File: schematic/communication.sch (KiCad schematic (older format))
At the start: 12 parts

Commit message: prototype footprint and placement test
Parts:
- C10, C9: renamed from C?; footprint (none) -> Capacitor_SMD:C_0805_2012Metric_Pad1.15x1.40mm_HandSolder
- J18: renamed from J?; footprint (none) -> Connector_PinHeader_2.54mm:PinHeader_1x02_P2.54mm_Vertical
- J19: renamed from J?; footprint (none) -> Connector_JST:JST_XH_B2B-XH-AM_1x02_P2.50mm_Vertical
- R17, R18, R19, R20, R21, R22, R23: renamed from R?; footprint (none) -> Resistor_SMD:R_0805_2012Metric_Pad1.15x1.40mm_HandSolder
- U5: renamed from U?; footprint (none) -> Package_SO:SOIC-8_3.9x4.9mm_P1.27mm
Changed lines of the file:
@@
 P 5400 3900
 AR Path="/5EFB8F98" Ref="U?"  Part="1"
-AR Path="/5EFB4D6F/5EFB8F98" Ref="U?"  Part="1"
-F 0 "U?" H 5500 4500 50  0000 C CNN
+AR Path="/5EFB4D6F/5EFB8F98" Ref="U5"  Part="1"
+F 0 "U5" H 5500 4500 50  0000 C CNN
 F 1 "MAX485E" H 5600 4400 50  0000 C CNN
-F 2 "" H 5400 3200 50  0001 C CNN
+F 2 "Package_SO:SOIC-8_3.9x4.9mm_P1.27mm" H 5400 3200 50  0001 C CNN
 F 3 "https://datasheets.maximintegrated.com/en/ds/MAX1487E-MAX491E.pdf" H 5400 3950 50  0001 C CNN
 	1    5400 3900
@@
 P 7150 3800
 AR Path="/5EFB8F9E" Ref="J?"  Part="1"
-AR Path="/5EFB4D6F/5EFB8F9E" Ref="J?"  Part="1"
-F 0 "J?" H 7230 3792 50  0000 L CNN
+AR Path="/5EFB4D6F/5EFB8F9E" Ref="J19"  Part="1"
+F 0 "J19" H 7230 3792 50  0000 L CNN
 F 1 "Conn_01x02" H 7230 3701 50  0000 L CNN
-F 2 "" H 7150 3800 50  0001 C CNN
+F 2 "Connector_JST:JST_XH_B2B-XH-AM_1x02_P2.50mm_Vertical" H 7150 3800 50  0001 C CNN
 F 3 "~" H 7150 3800 50  0001 C CNN
 	1    7150 3800
@@
 P 6200 4400
 AR Path="/5EFB8FA4" Ref="#PWR?"  Part="1"
-AR Path="/5EFB4D6F/5EFB8FA4" Ref="#PWR?"  Part="1"
-F 0 "#PWR?" H 6200 4250 50  0001 C CNN
+AR Path="/5EFB4D6F/5EFB8FA4" Ref="#PWR060"  Part="1"
+F 0 "#PWR060" H 6200 4250 50  0001 C CNN
 F 1 "+3.3V" H 6215 4573 50  0000 C CNN
 F 2 "" H 6200 4400 50  0001 C CNN
@@
 P 6200 3500
 AR Path="/5EFB8FAA" Ref="#PWR?"  Part="1"
-AR Path="/5EFB4D6F/5EFB8FAA" Ref="#PWR?"  Part="1"
-F 0 "#PWR?" H 6200 3250 50  0001 C CNN
+AR Path="/5EFB4D6F/5EFB8FAA" Ref="#PWR059"  Part="1"
+F 0 "#PWR059" H 6200 3250 50  0001 C CNN
 F 1 "GND" H 6205 3327 50  0000 C CNN
 F 2 "" H 6200 3500 50  0001 C CNN
@@
 P 6200 3650
 AR Path="/5EFB8FB0" Ref="R?"  Part="1"
-AR Path="/5EFB4D6F/5EFB8FB0" Ref="R?"  Part="1"
-F 0 "R?" H 6270 3696 50  0000 L CNN
+AR Path="/5EFB4D6F/5EFB8FB0" Ref="R21"  Part="1"
+F 0 "R21" H 6270 3696 50  0000 L CNN
 F 1 "20K" H 6270 3605 50  0000 L CNN
-F 2 "" V 6130 3650 50  0001 C CNN
+F 2 "Resistor_SMD:R_0805_2012Metric_Pad1.15x1.40mm_HandSolder" V 6130 3650 50  0001 C CNN
 F 3 "~" H 6200 3650 50  0001 C CNN
 	1    6200 3650
@@
 P 6200 4250
 AR Path="/5EFB8FB6" Ref="R?"  Part="1"
-AR Path="/5EFB4D6F/5EFB8FB6" Ref="R?"  Part="1"
-F 0 "R?" H 6270 4296 50  0000 L CNN
+AR Path="/5EFB4D6F/5EFB8FB6" Ref="R22"  Part="1"
+F 0 "R22" H 6270 4296 50  0000 L CNN
 F 1 "20K" H 6270 4205 50  0000 L CNN
-F 2 "" V 6130 4250 50  0001 C CNN
+F 2 "Resistor_SMD:R_0805_2012Metric_Pad1.15x1.40mm_HandSolder" V 6130 4250 50  0001 C CNN
 F 3 "~" H 6200 4250 50  0001 C CNN
 	1    6200 4250
@@
 P 5400 4500
 AR Path="/5EFB8FBD" Ref="#PWR?"  Part="1"
-AR Path="/5EFB4D6F/5EFB8FBD" Ref="#PWR?"  Part="1"
-F 0 "#PWR?" H 5400 4250 50  0001 C CNN
+AR Path="/5EFB4D6F/5EFB8FBD" Ref="#PWR058"  Part="1"
+F 0 "#PWR058" H 5400 4250 50  0001 C CNN
 F 1 "GND" H 5405 4327 50  0000 C CNN
 F 2 "" H 5400 4500 50  0001 C CNN
@@
 P 6450 3450
 AR Path="/5EFB8FC6" Ref="R?"  Part="1"
-AR Path="/5EFB4D6F/5EFB8FC6" Ref="R?"  Part="1"
-F 0 "R?" H 6520 3496 50  0000 L CNN
+AR Path="/5EFB4D6F/5EFB8FC6" Ref="R23"  Part="1"
+F 0 "R23" H 6520 3496 50  0000 L CNN
 F 1 "120" H 6520 3405 50  0000 L CNN
-F 2 "" V 6380 3450 50  0001 C CNN
+F 2 "Resistor_SMD:R_0805_2012Metric_Pad1.15x1.40mm_HandSolder" V 6380 3450 50  0001 C CNN
 F 3 "~" H 6450 3450 50  0001 C CNN
 	1    6450 3450
@@
 P 4750 3550
 AR Path="/5EFB8FCF" Ref="R?"  Part="1"
-AR Path="/5EFB4D6F/5EFB8FCF" Ref="R?"  Part="1"
-F 0 "R?" H 4820 3596 50  0000 L CNN
+AR Path="/5EFB4D6F/5EFB8FCF" Ref="R20"  Part="1"
+F 0 "R20" H 4820 3596 50  0000 L CNN
 F 1 "10K" H 4820 3505 50  0000 L CNN
-F 2 "" V 4680 3550 50  0001 C CNN
+F 2 "Resistor_SMD:R_0805_2012Metric_Pad1.15x1.40mm_HandSolder" V 4680 3550 50  0001 C CNN
 F 3 "~" H 4750 3550 50  0001 C CNN
 	1    4750 3550
@@
 P 4600 3550
 AR Path="/5EFB8FD5" Ref="R?"  Part="1"
-AR Path="/5EFB4D6F/5EFB8FD5" Ref="R?"  Part="1"
-F 0 "R?" H 4670 3596 50  0000 L CNN
+AR Path="/5EFB4D6F/5EFB8FD5" Ref="R19"  Part="1"
+F 0 "R19" H 4670 3596 50  0000 L CNN
 F 1 "10K" H 4670 3505 50  0000 L CNN
-F 2 "" V 4530 3550 50  0001 C CNN
+F 2 "Resistor_SMD:R_0805_2012Metric_Pad1.15x1.40mm_HandSolder" V 4530 3550 50  0001 C CNN
 F 3 "~" H 4600 3550 50  0001 C CNN
 	1    4600 3550
@@
 P 4450 3550
 AR Path="/5EFB8FDB" Ref="R?"  Part="1"
-AR Path="/5EFB4D6F/5EFB8FDB" Ref="R?"  Part="1"
-F 0 "R?" H 4520 3596 50  0000 L CNN
+AR Path="/5EFB4D6F/5EFB8FDB" Ref="R18"  Part="1"
+F 0 "R18" H 4520 3596 50  0000 L CNN
 F 1 "10K" H 4520 3505 50  0000 L CNN
-F 2 "" V 4380 3550 50  0001 C CNN
+F 2 "Resistor_SMD:R_0805_2012Metric_Pad1.15x1.40mm_HandSolder" V 4380 3550 50  0001 C CNN
 F 3 "~" H 4450 3550 50  0001 C CNN
 	1    4450 3550
@@
 P 4300 3550
 AR Path="/5EFB8FE1" Ref="R?"  Part="1"
-AR Path="/5EFB4D6F/5EFB8FE1" Ref="R?"  Part="1"
-F 0 "R?" H 4370 3596 50  0000 L CNN
+AR Path="/5EFB4D6F/5EFB8FE1" Ref="R17"  Part="1"
+F 0 "R17" H 4370 3596 50  0000 L CNN
 F 1 "10K" H 4370 3505 50  0000 L CNN
-F 2 "" V 4230 3550 50  0001 C CNN
+F 2 "Resistor_SMD:R_0805_2012Metric_Pad1.15x1.40mm_HandSolder" V 4230 3550 50  0001 C CNN
 F 3 "~" H 4300 3550 50  0001 C CNN
 	1    4300 3550
@@
 P 4550 3400
 AR Path="/5EFB9000" Ref="#PWR?"  Part="1"
-AR Path="/5EFB4D6F/5EFB9000" Ref="#PWR?"  Part="1"
-F 0 "#PWR?" H 4550 3250 50  0001 C CNN
+AR Path="/5EFB4D6F/5EFB9000" Ref="#PWR054"  Part="1"
+F 0 "#PWR054" H 4550 3250 50  0001 C CNN
 F 1 "+3.3V" H 4565 3573 50  0000 C CNN
 F 2 "" H 4550 3400 50  0001 C CNN
@@
 P 6900 3400
 AR Path="/5EFB9026" Ref="J?"  Part="1"
-AR Path="/5EFB4D6F/5EFB9026" Ref="J?"  Part="1"
-F 0 "J?" H 6872 3282 50  0000 R CNN
+AR Path="/5EFB4D6F/5EFB9026" Ref="J18"  Part="1"
+F 0 "J18" H 6872 3282 50  0000 R CNN
 F 1 "Conn_01x02_Male" H 6872 3373 50  0000 R CNN
-F 2 "" H 6900 3400 50  0001 C CNN
+F 2 "Connector_PinHeader_2.54mm:PinHeader_1x02_P2.54mm_Vertical" H 6900 3400 50  0001 C CNN
 F 3 "~" H 6900 3400 50  0001 C CNN
 	1    6900 3400
@@
 P 5350 2850
 AR Path="/5EFB900E" Ref="C?"  Part="1"
-AR Path="/5EFB4D6F/5EFB900E" Ref="C?"  Part="1"
-F 0 "C?" H 5465 2896 50  0000 L CNN
+AR Path="/5EFB4D6F/5EFB900E" Ref="C10"  Part="1"
+F 0 "C10" H 5465 2896 50  0000 L CNN
 F 1 "0.1uF" H 5465 2805 50  0000 L CNN
-F 2 "" H 5388 2700 50  0001 C CNN
+F 2 "Capacitor_SMD:C_0805_2012Metric_Pad1.15x1.40mm_HandSolder" H 5388 2700 50  0001 C CNN
 F 3 "~" H 5350 2850 50  0001 C CNN
 	1    5350 2850
@@
 P 4900 2850
 AR Path="/5EFB9008" Ref="C?"  Part="1"
-AR Path="/5EFB4D6F/5EFB9008" Ref="C?"  Part="1"
-F 0 "C?" H 5015 2896 50  0000 L CNN
+AR Path="/5EFB4D6F/5EFB9008" Ref="C9"  Part="1"
+F 0 "C9" H 5015 2896 50  0000 L CNN
 F 1 "10uF" H 5015 2805 50  0000 L CNN
-F 2 "" H 4938 2700 50  0001 C CNN
+F 2 "Capacitor_SMD:C_0805_2012Metric_Pad1.15x1.40mm_HandSolder" H 4938 2700 50  0001 C CNN
 F 3 "~" H 4900 2850 50  0001 C CNN
 	1    4900 2850
@@
 P 5150 2700
 AR Path="/5EFB9014" Ref="#PWR?"  Part="1"
-AR Path="/5EFB4D6F/5EFB9014" Ref="#PWR?"  Part="1"
-F 0 "#PWR?" H 5150 2550 50  0001 C CNN
+AR Path="/5EFB4D6F/5EFB9014" Ref="#PWR055"  Part="1"
+F 0 "#PWR055" H 5150 2550 50  0001 C CNN
 F 1 "+3.3V" H 5165 2873 50  0000 C CNN
 F 2 "" H 5150 2700 50  0001 C CNN
@@
 P 5150 3000
 AR Path="/5EFB901A" Ref="#PWR?"  Part="1"
-AR Path="/5EFB4D6F/5EFB901A" Ref="#PWR?"  Part="1"
-F 0 "#PWR?" H 5150 2750 50  0001 C CNN
+AR Path="/5EFB4D6F/5EFB901A" Ref="#PWR056"  Part="1"
+F 0 "#PWR056" H 5150 2750 50  0001 C CNN
 F 1 "GND" H 5155 2827 50  0000 C CNN
 F 2 "" H 5150 3000 50  0001 C CNN
@@
 P 5400 3400
 AR Path="/5EFB9039" Ref="#PWR?"  Part="1"
-AR Path="/5EFB4D6F/5EFB9039" Ref="#PWR?"  Part="1"
-F 0 "#PWR?" H 5400 3250 50  0001 C CNN
+AR Path="/5EFB4D6F/5EFB9039" Ref="#PWR057"  Part="1"
+F 0 "#PWR057" H 5400 3250 50  0001 C CNN
 F 1 "+3.3V" H 5415 3573 50  0000 C CNN
 F 2 "" H 5400 3400 50  0001 C CNN

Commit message: new pcb design
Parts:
- J19: footprint Connector_JST:JST_XH_B2B-XH-AM_1x02_P2.50mm_Vertical -> Connector_JST:JST_XH_B2B-XH-A_1x02_P2.50mm_Vertical
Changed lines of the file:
@@
 F 0 "J19" H 7230 3792 50  0000 L CNN
 F 1 "Conn_01x02" H 7230 3701 50  0000 L CNN
-F 2 "Connector_JST:JST_XH_B2B-XH-AM_1x02_P2.50mm_Vertical" H 7150 3800 50  0001 C CNN
+F 2 "Connector_JST:JST_XH_B2B-XH-A_1x02_P2.50mm_Vertical" H 7150 3800 50  0001 C CNN
 F 3 "~" H 7150 3800 50  0001 C CNN
 	1    7150 3800

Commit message: SP385 instead of MAX
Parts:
- removed U5: MAX485E, Package_SO:SOIC-8_3.9x4.9mm_P1.27mm, symbol Interface_UART:MAX485E
- added U?: SP3485CN, Package_SO:SOIC-8_3.9x4.9mm_P1.27mm, symbol Interface_UART:SP3485CN
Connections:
- wire segments 34 -> 42
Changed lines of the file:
@@
 $EndDescr
-$Comp
-L Interface_UART:MAX485E U?
-U 1 1 5EFB8F98
-P 5400 3900
-AR Path="/5EFB8F98" Ref="U?"  Part="1"
-AR Path="/5EFB4D6F/5EFB8F98" Ref="U5"  Part="1"
-F 0 "U5" H 5500 4500 50  0000 C CNN
-F 1 "MAX485E" H 5600 4400 50  0000 C CNN
-F 2 "Package_SO:SOIC-8_3.9x4.9mm_P1.27mm" H 5400 3200 50  0001 C CNN
-F 3 "https://datasheets.maximintegrated.com/en/ds/MAX1487E-MAX491E.pdf" H 5400 3950 50  0001 C CNN
-	1    5400 3900
-	1    0    0    -1
-$EndComp
 $Comp
 L Connector_Generic:Conn_01x02 J?
@@
 Wire Wire Line
 	6450 4100 6700 4100
+Text GLabel 6950 3800 1    50   Input ~ 0
+RS485-A
 Text GLabel 6950 3900 3    50   Input ~ 0
-RS485-A
-Text GLabel 6950 3800 1    50   Input ~ 0
 RS485-B
 Wire Wire Line
@@
 	1    0    0    -1
 $EndComp
+$Comp
+L Interface_UART:SP3485CN U?
+U 1 1 5EEA53A1
+P 5400 3950
+F 0 "U?" H 5400 4531 50  0000 C CNN
+F 1 "SP3485CN" H 5400 4440 50  0000 C CNN
+F 2 "Package_SO:SOIC-8_3.9x4.9mm_P1.27mm" H 6450 3600 50  0001 C CIN
+F 3 "http://www.icbase.com/pdf/SPX/SPX00480106.pdf" H 5400 3950 50  0001 C CNN
+	1    5400 3950
+	1    0    0    -1
+$EndComp
+Wire Wire Line
+	5800 3850 5800 3800
+Wire Wire Line
+	5800 4050 5800 4100
+Wire Wire Line
+	5000 4100 5000 4150
+Wire Wire Line
+	5000 4050 5000 4000
+Wire Wire Line
+	5000 3850 5000 3900
+Wire Wire Line
+	5000 3800 5000 3750
+Wire Wire Line
+	5400 3550 5400 3400
+Wire Wire Line
+	5400 4350 5400 4500
 $EndSCHEMATC

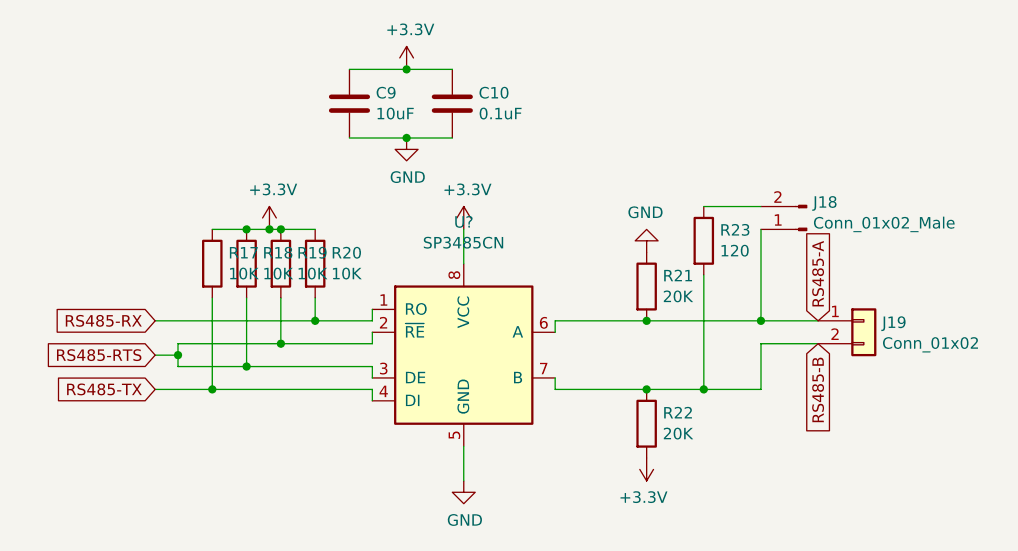
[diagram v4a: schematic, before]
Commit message: added 5v boost converter
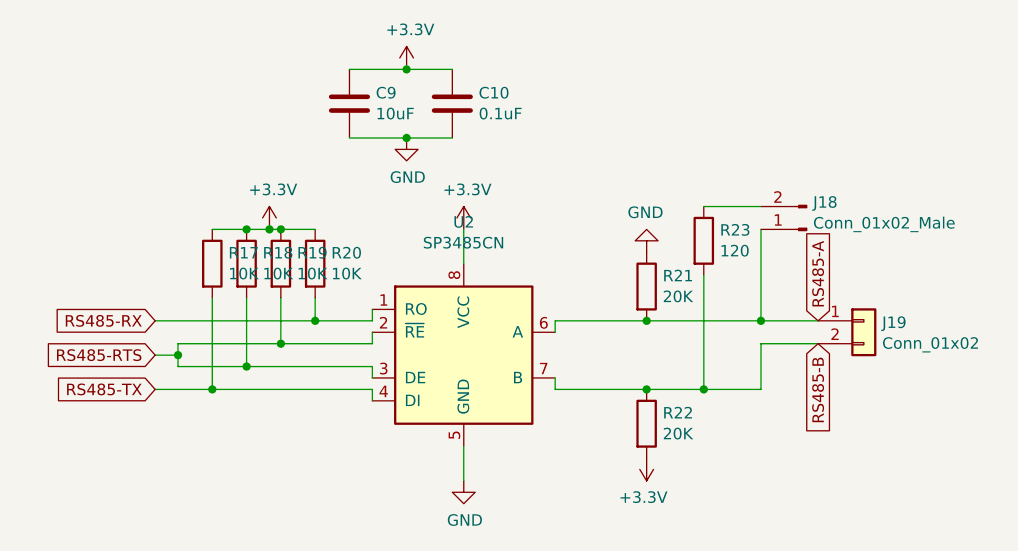
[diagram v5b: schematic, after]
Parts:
- gave numbers to parts that had none: 1
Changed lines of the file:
@@
 $Descr A4 11693 8268
 encoding utf-8
-Sheet 6 5
+Sheet 5 5
 Title ""
 Date ""
@@
 $EndComp
 $Comp
-L Interface_UART:SP3485CN U?
+L Interface_UART:SP3485CN U2
 U 1 1 5EEA53A1
 P 5400 3950
-F 0 "U?" H 5400 4531 50  0000 C CNN
+F 0 "U2" H 5400 4531 50  0000 C CNN
 F 1 "SP3485CN" H 5400 4440 50  0000 C CNN
 F 2 "Package_SO:SOIC-8_3.9x4.9mm_P1.27mm" H 6450 3600 50  0001 C CIN

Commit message: boost converter on Apsu board and PCB design
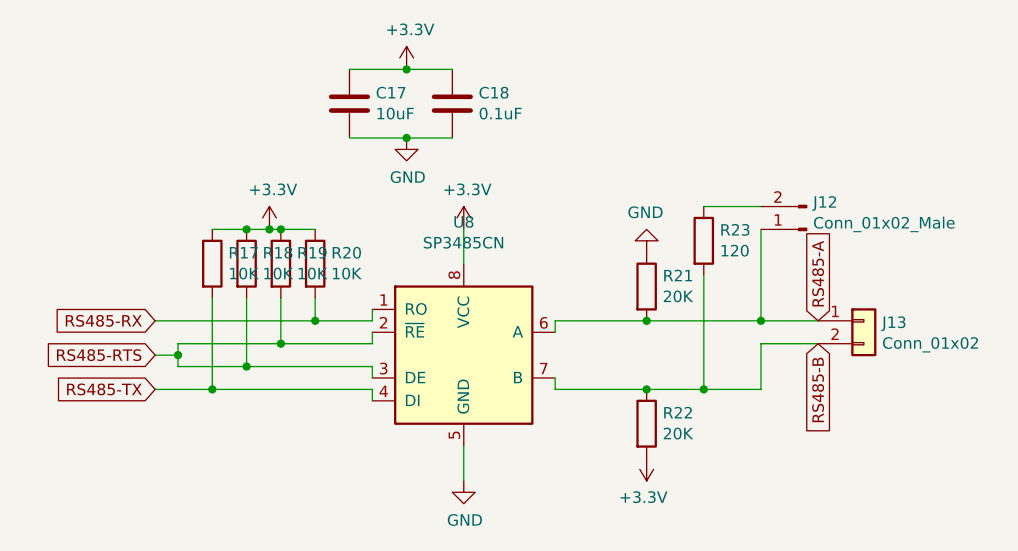
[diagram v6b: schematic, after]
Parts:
- renumbered C9 to C17, C10 to C18, J18 to J12, J19 to J13, U2 to U8
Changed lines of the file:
@@
 P 7150 3800
 AR Path="/5EFB8F9E" Ref="J?"  Part="1"
-AR Path="/5EFB4D6F/5EFB8F9E" Ref="J19"  Part="1"
-F 0 "J19" H 7230 3792 50  0000 L CNN
+AR Path="/5EFB4D6F/5EFB8F9E" Ref="J13"  Part="1"
+F 0 "J13" H 7230 3792 50  0000 L CNN
 F 1 "Conn_01x02" H 7230 3701 50  0000 L CNN
 F 2 "Connector_JST:JST_XH_B2B-XH-A_1x02_P2.50mm_Vertical" H 7150 3800 50  0001 C CNN
@@
 P 6200 4400
 AR Path="/5EFB8FA4" Ref="#PWR?"  Part="1"
-AR Path="/5EFB4D6F/5EFB8FA4" Ref="#PWR060"  Part="1"
-F 0 "#PWR060" H 6200 4250 50  0001 C CNN
+AR Path="/5EFB4D6F/5EFB8FA4" Ref="#PWR073"  Part="1"
+F 0 "#PWR073" H 6200 4250 50  0001 C CNN
 F 1 "+3.3V" H 6215 4573 50  0000 C CNN
 F 2 "" H 6200 4400 50  0001 C CNN
@@
 P 6200 3500
 AR Path="/5EFB8FAA" Ref="#PWR?"  Part="1"
-AR Path="/5EFB4D6F/5EFB8FAA" Ref="#PWR059"  Part="1"
-F 0 "#PWR059" H 6200 3250 50  0001 C CNN
+AR Path="/5EFB4D6F/5EFB8FAA" Ref="#PWR072"  Part="1"
+F 0 "#PWR072" H 6200 3250 50  0001 C CNN
 F 1 "GND" H 6205 3327 50  0000 C CNN
 F 2 "" H 6200 3500 50  0001 C CNN
@@
 P 5400 4500
 AR Path="/5EFB8FBD" Ref="#PWR?"  Part="1"
-AR Path="/5EFB4D6F/5EFB8FBD" Ref="#PWR058"  Part="1"
-F 0 "#PWR058" H 5400 4250 50  0001 C CNN
+AR Path="/5EFB4D6F/5EFB8FBD" Ref="#PWR071"  Part="1"
+F 0 "#PWR071" H 5400 4250 50  0001 C CNN
 F 1 "GND" H 5405 4327 50  0000 C CNN
 F 2 "" H 5400 4500 50  0001 C CNN
@@
 P 4550 3400
 AR Path="/5EFB9000" Ref="#PWR?"  Part="1"
-AR Path="/5EFB4D6F/5EFB9000" Ref="#PWR054"  Part="1"
-F 0 "#PWR054" H 4550 3250 50  0001 C CNN
+AR Path="/5EFB4D6F/5EFB9000" Ref="#PWR067"  Part="1"
+F 0 "#PWR067" H 4550 3250 50  0001 C CNN
 F 1 "+3.3V" H 4565 3573 50  0000 C CNN
 F 2 "" H 4550 3400 50  0001 C CNN
@@
 P 6900 3400
 AR Path="/5EFB9026" Ref="J?"  Part="1"
-AR Path="/5EFB4D6F/5EFB9026" Ref="J18"  Part="1"
-F 0 "J18" H 6872 3282 50  0000 R CNN
+AR Path="/5EFB4D6F/5EFB9026" Ref="J12"  Part="1"
+F 0 "J12" H 6872 3282 50  0000 R CNN
 F 1 "Conn_01x02_Male" H 6872 3373 50  0000 R CNN
 F 2 "Connector_PinHeader_2.54mm:PinHeader_1x02_P2.54mm_Vertical" H 6900 3400 50  0001 C CNN
@@
 P 5350 2850
 AR Path="/5EFB900E" Ref="C?"  Part="1"
-AR Path="/5EFB4D6F/5EFB900E" Ref="C10"  Part="1"
-F 0 "C10" H 5465 2896 50  0000 L CNN
+AR Path="/5EFB4D6F/5EFB900E" Ref="C18"  Part="1"
+F 0 "C18" H 5465 2896 50  0000 L CNN
 F 1 "0.1uF" H 5465 2805 50  0000 L CNN
 F 2 "Capacitor_SMD:C_0805_2012Metric_Pad1.15x1.40mm_HandSolder" H 5388 2700 50  0001 C CNN
@@
 P 4900 2850
 AR Path="/5EFB9008" Ref="C?"  Part="1"
-AR Path="/5EFB4D6F/5EFB9008" Ref="C9"  Part="1"
-F 0 "C9" H 5015 2896 50  0000 L CNN
+AR Path="/5EFB4D6F/5EFB9008" Ref="C17"  Part="1"
+F 0 "C17" H 5015 2896 50  0000 L CNN
 F 1 "10uF" H 5015 2805 50  0000 L CNN
 F 2 "Capacitor_SMD:C_0805_2012Metric_Pad1.15x1.40mm_HandSolder" H 4938 2700 50  0001 C CNN
@@
 P 5150 2700
 AR Path="/5EFB9014" Ref="#PWR?"  Part="1"
-AR Path="/5EFB4D6F/5EFB9014" Ref="#PWR055"  Part="1"
-F 0 "#PWR055" H 5150 2550 50  0001 C CNN
+AR Path="/5EFB4D6F/5EFB9014" Ref="#PWR068"  Part="1"
+F 0 "#PWR068" H 5150 2550 50  0001 C CNN
 F 1 "+3.3V" H 5165 2873 50  0000 C CNN
 F 2 "" H 5150 2700 50  0001 C CNN
@@
 P 5150 3000
 AR Path="/5EFB901A" Ref="#PWR?"  Part="1"
-AR Path="/5EFB4D6F/5EFB901A" Ref="#PWR056"  Part="1"
-F 0 "#PWR056" H 5150 2750 50  0001 C CNN
+AR Path="/5EFB4D6F/5EFB901A" Ref="#PWR069"  Part="1"
+F 0 "#PWR069" H 5150 2750 50  0001 C CNN
 F 1 "GND" H 5155 2827 50  0000 C CNN
 F 2 "" H 5150 3000 50  0001 C CNN
@@
 P 5400 3400
 AR Path="/5EFB9039" Ref="#PWR?"  Part="1"
-AR Path="/5EFB4D6F/5EFB9039" Ref="#PWR057"  Part="1"
-F 0 "#PWR057" H 5400 3250 50  0001 C CNN
+AR Path="/5EFB4D6F/5EFB9039" Ref="#PWR070"  Part="1"
+F 0 "#PWR070" H 5400 3250 50  0001 C CNN
 F 1 "+3.3V" H 5415 3573 50  0000 C CNN
 F 2 "" H 5400 3400 50  0001 C CNN
@@
 $EndComp
 $Comp
-L Interface_UART:SP3485CN U2
+L Interface_UART:SP3485CN U8
 U 1 1 5EEA53A1
 P 5400 3950
-F 0 "U2" H 5400 4531 50  0000 C CNN
+F 0 "U8" H 5400 4531 50  0000 C CNN
 F 1 "SP3485CN" H 5400 4440 50  0000 C CNN
 F 2 "Package_SO:SOIC-8_3.9x4.9mm_P1.27mm" H 6450 3600 50  0001 C CIN

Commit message: added MPN
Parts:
- C17: MPN (none) -> C0805C106K8PACTU
- C18: MPN (none) -> C0805C104J5RACTU
- R17, R18, R19, R20: MPN (none) -> ERA-6AEB103V
- R21, R22: MPN (none) -> ERA6AEB203V
- R23: MPN (none) -> ERJ-6ENF1200V
- U8: MPN (none) -> MAX485CSA+
